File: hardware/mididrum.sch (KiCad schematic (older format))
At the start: 30 parts

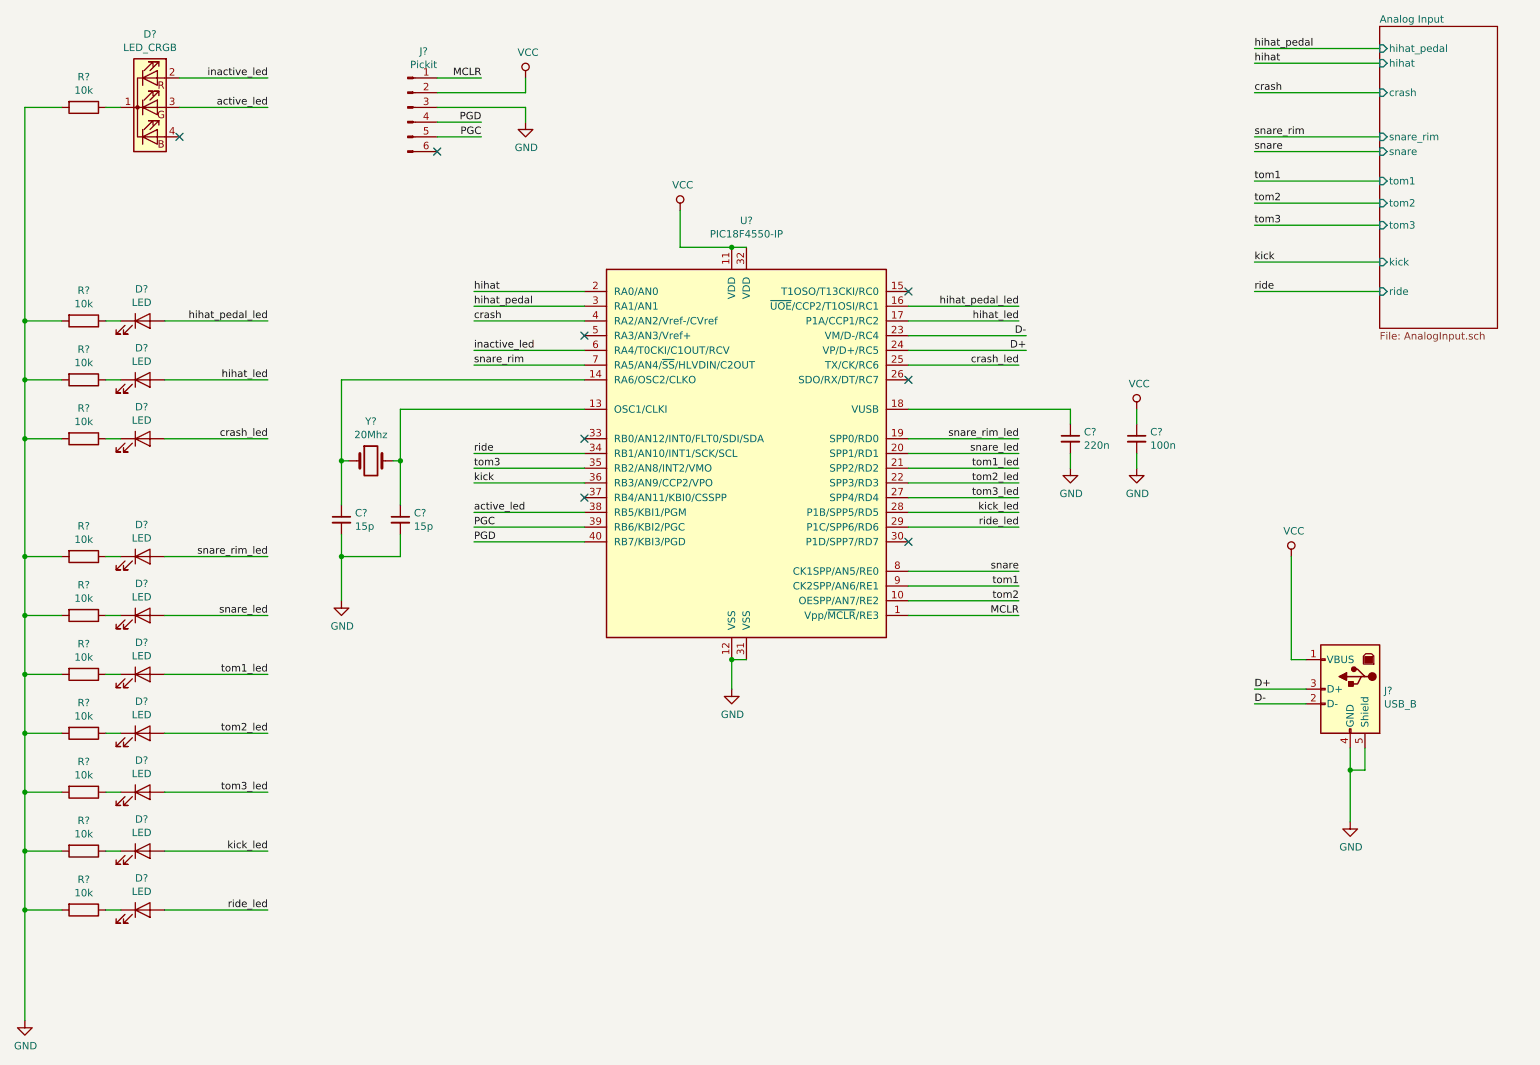
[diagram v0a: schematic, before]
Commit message: Update board
simplify analog input
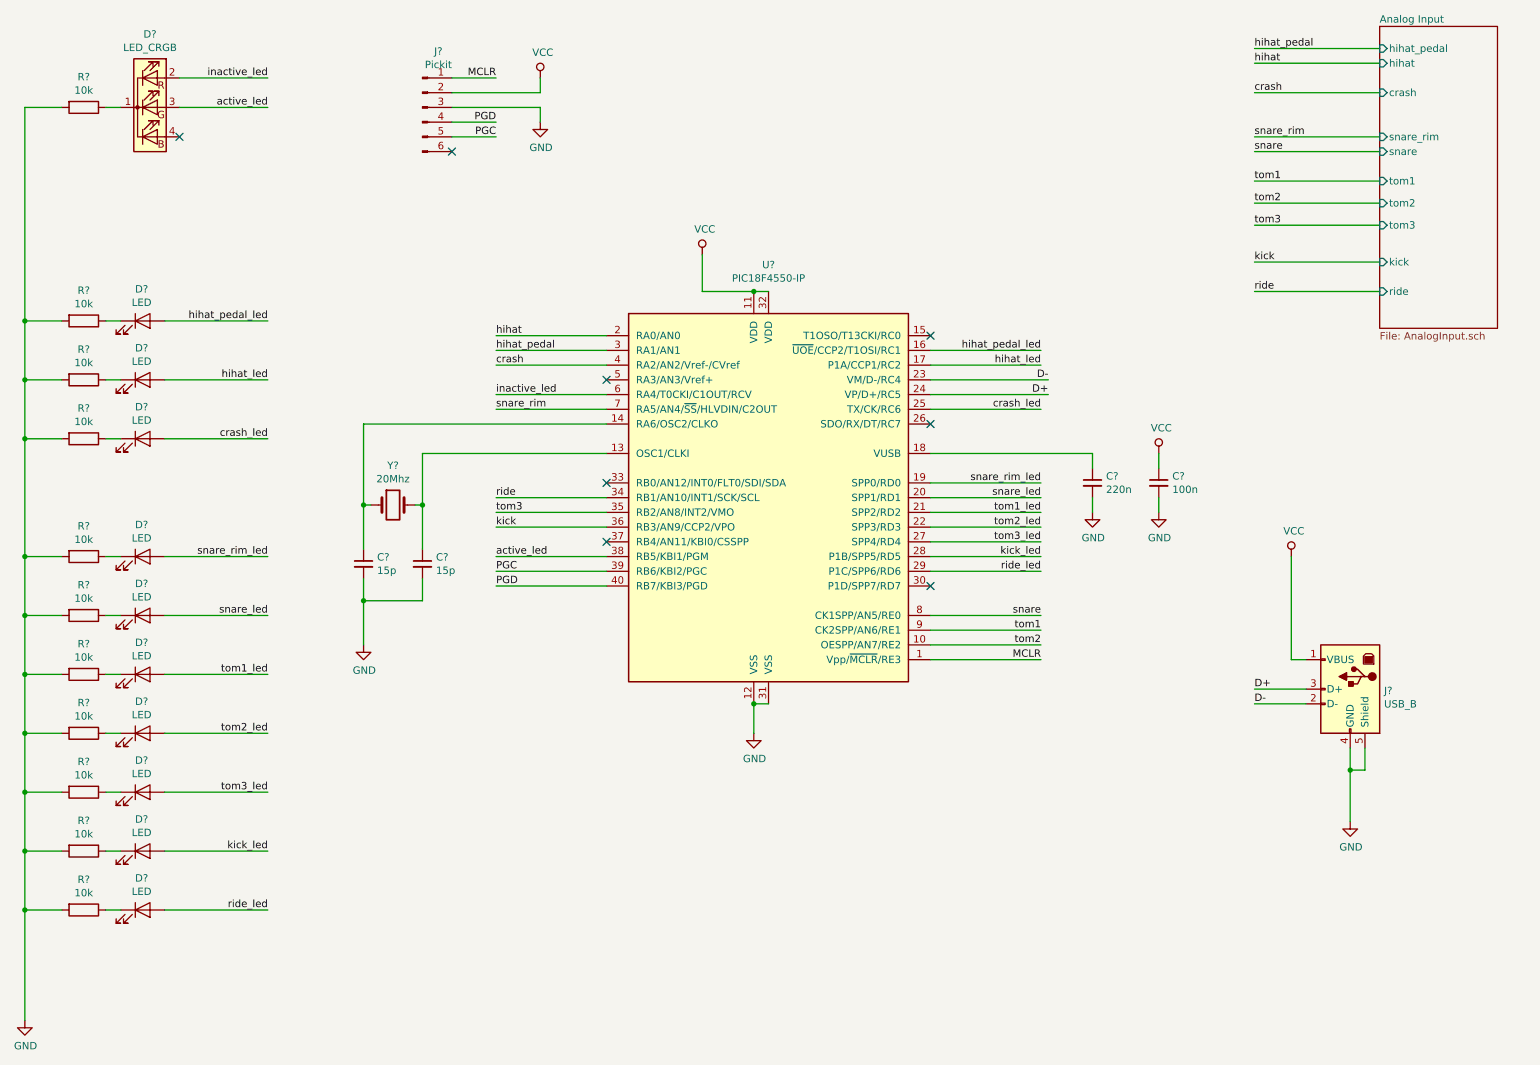
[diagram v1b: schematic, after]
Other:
- moved on the sheet: C?, J?, U?, Y?
